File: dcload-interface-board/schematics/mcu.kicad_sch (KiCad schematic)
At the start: 21 parts, among them J200 SWD, J201 UART, U200 RP2040, U201 W25Q16JV, Y200 12MHz

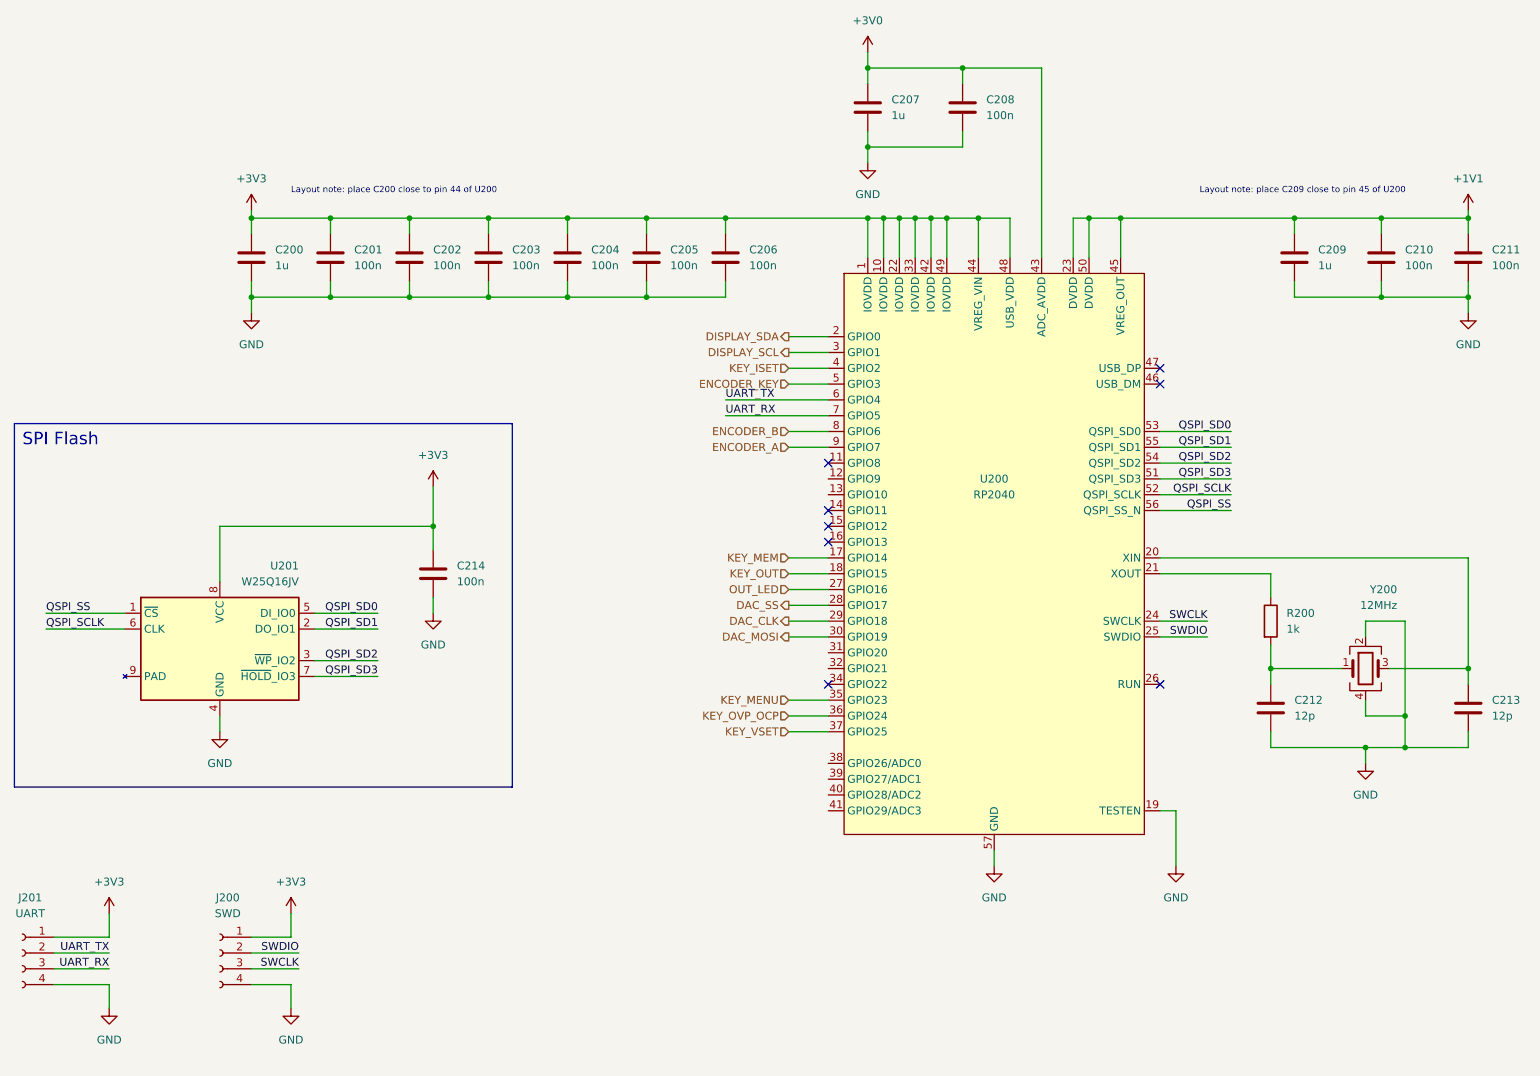
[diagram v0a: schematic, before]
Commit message: add: interface panel board
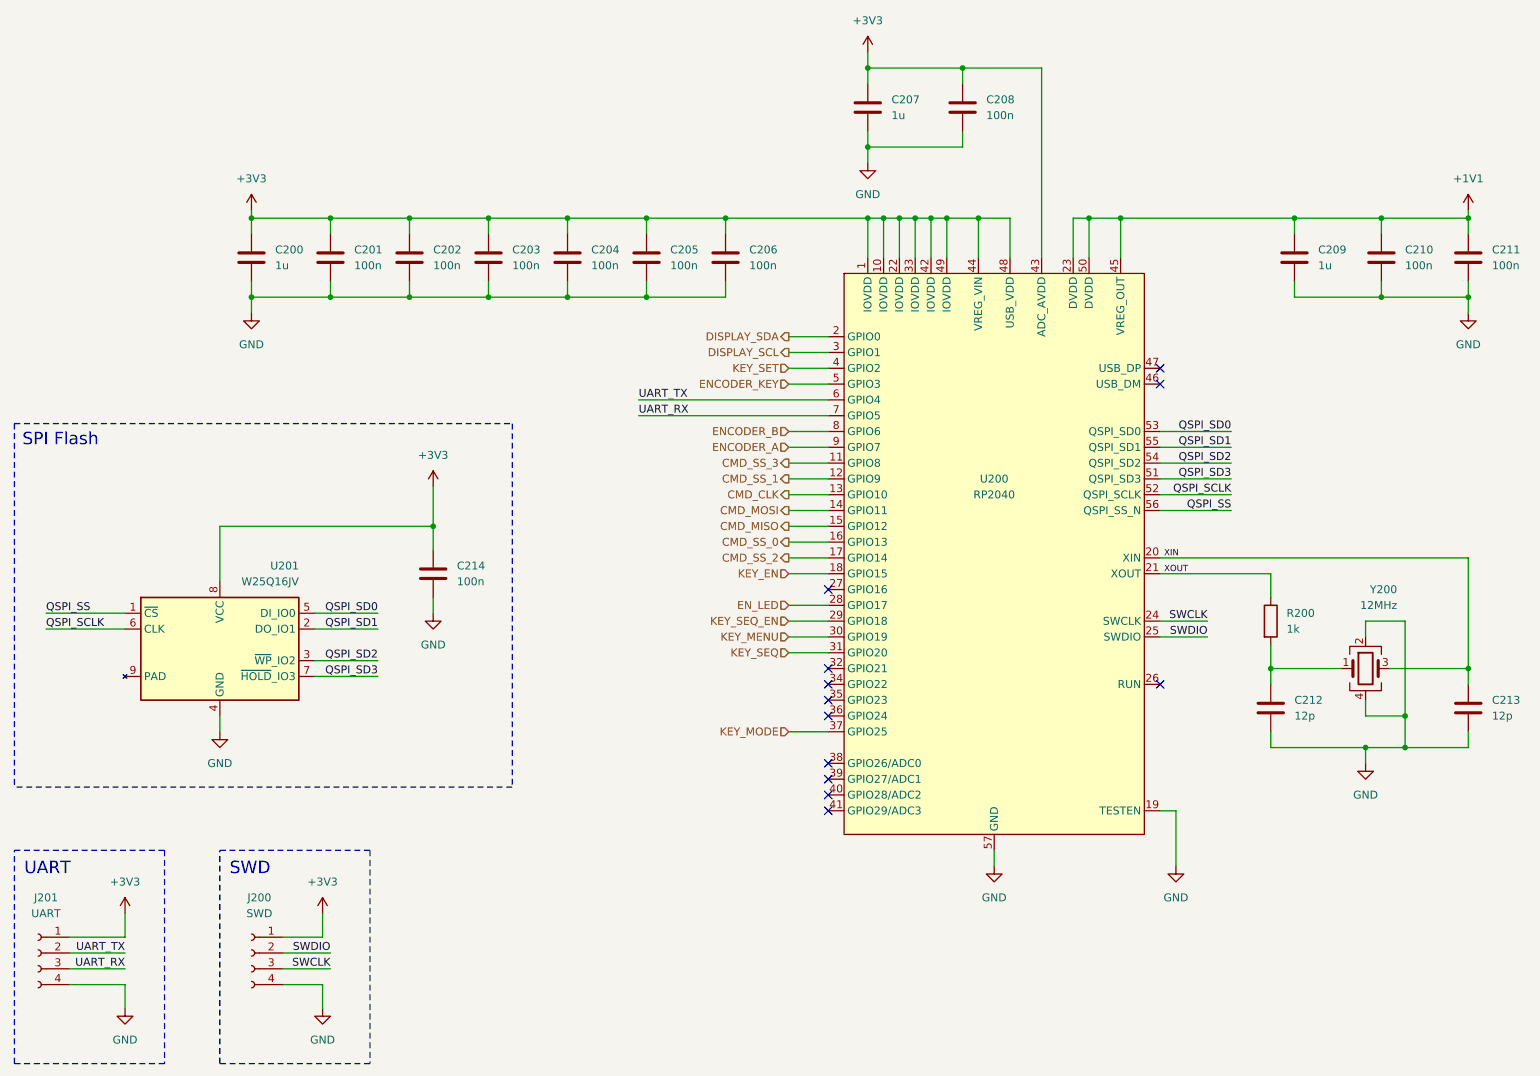
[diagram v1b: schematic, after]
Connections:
- net +3V0 is gone; now on net +3V3: C207.1, C208.1, U200.43 (ADC_AVDD)
- net DAC_MOSI is gone; now on net KEY_MENU: U200.30 (GPIO19)
- net KEY_MENU: no longer U200.35 (GPIO23)
- net CMD_SS_3: now reaches U200.11 (GPIO8)
- net CMD_SS_1: now reaches U200.12 (GPIO9)
- net CMD_CLK: now reaches U200.13 (GPIO10)
- net CMD_MOSI: now reaches U200.14 (GPIO11)
- net CMD_MISO: now reaches U200.15 (GPIO12)
- net CMD_SS_0: now reaches U200.16 (GPIO13)
- net XIN: now reaches C213.1, U200.20 (XIN), Y200.3
- net XOUT: now reaches R200.1, U200.21 (XOUT)
- net KEY_SEQ: now reaches U200.31 (GPIO20)
- net DAC_CLK renamed KEY_SEQ_EN
- net DAC_SS renamed EN_LED
- net KEY_ISET renamed KEY_SET
- net KEY_MEM renamed CMD_SS_2
- net KEY_OUT renamed KEY_EN
- net KEY_OVP_OCP: no longer names the net of U200.36 (GPIO24)
- net KEY_VSET renamed KEY_MODE
- net OUT_LED: no longer names the net of U200.27 (GPIO16)
- no-connect marks 8 -> 12
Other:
- note removed: "Layout note: place C200 close to pin 44 of U200"
- note removed: "Layout note: place C209 close to pin 45 of U200"
- title: Linear PSU Digital Board -> MCU
- moved on the sheet: J200, J201
